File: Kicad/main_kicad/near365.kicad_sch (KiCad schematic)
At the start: 34 parts, among them J1 BMS power input, J2 USB_C_Receptacle_USB2.0_16P, SW1 Switch, SW2 Switch, SW3 SW_en, SW4 SW_boot, SW5 RotaryEncoder_Switch_MP, U1 ESP32-S3-WROOM-1, U2 TC00500, U3 CR2013-MI2120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

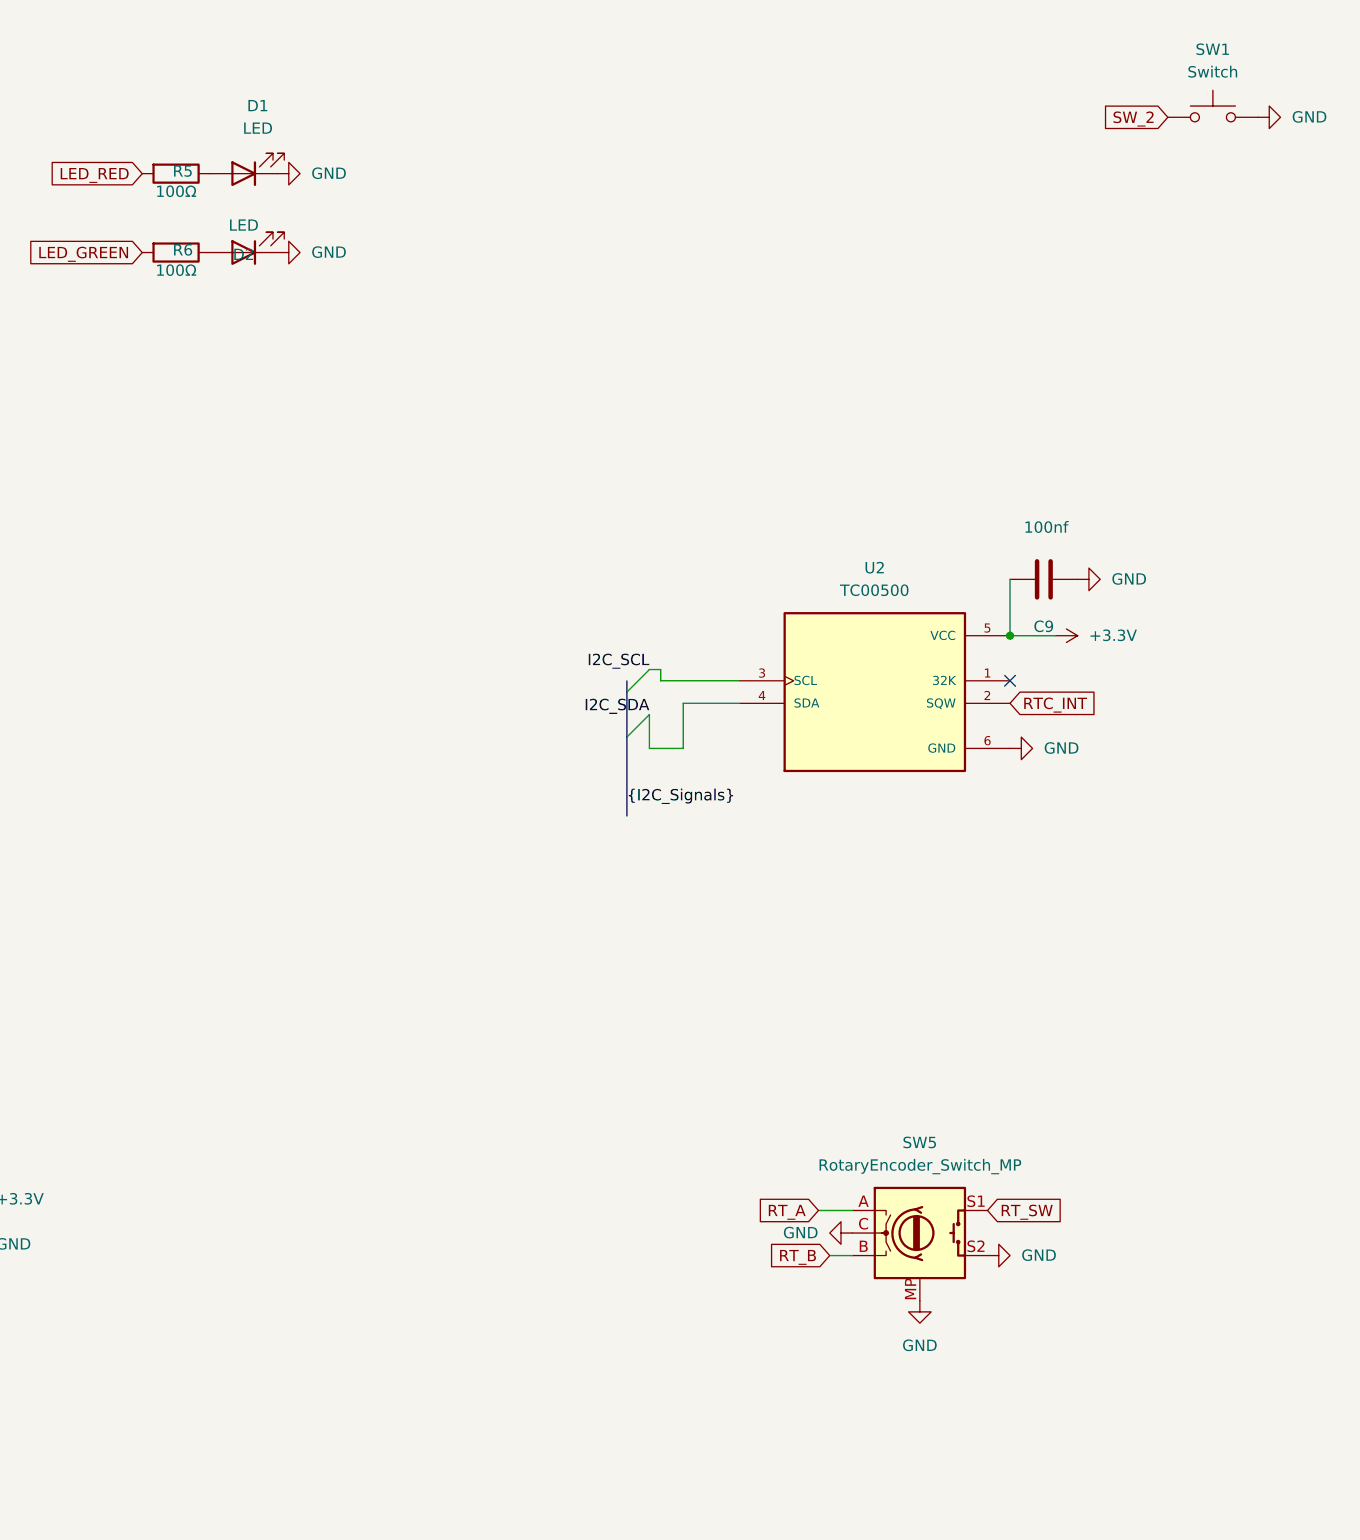
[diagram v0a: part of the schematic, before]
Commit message: Updated power, made changes to 3d front plate, added pull down r to encoder
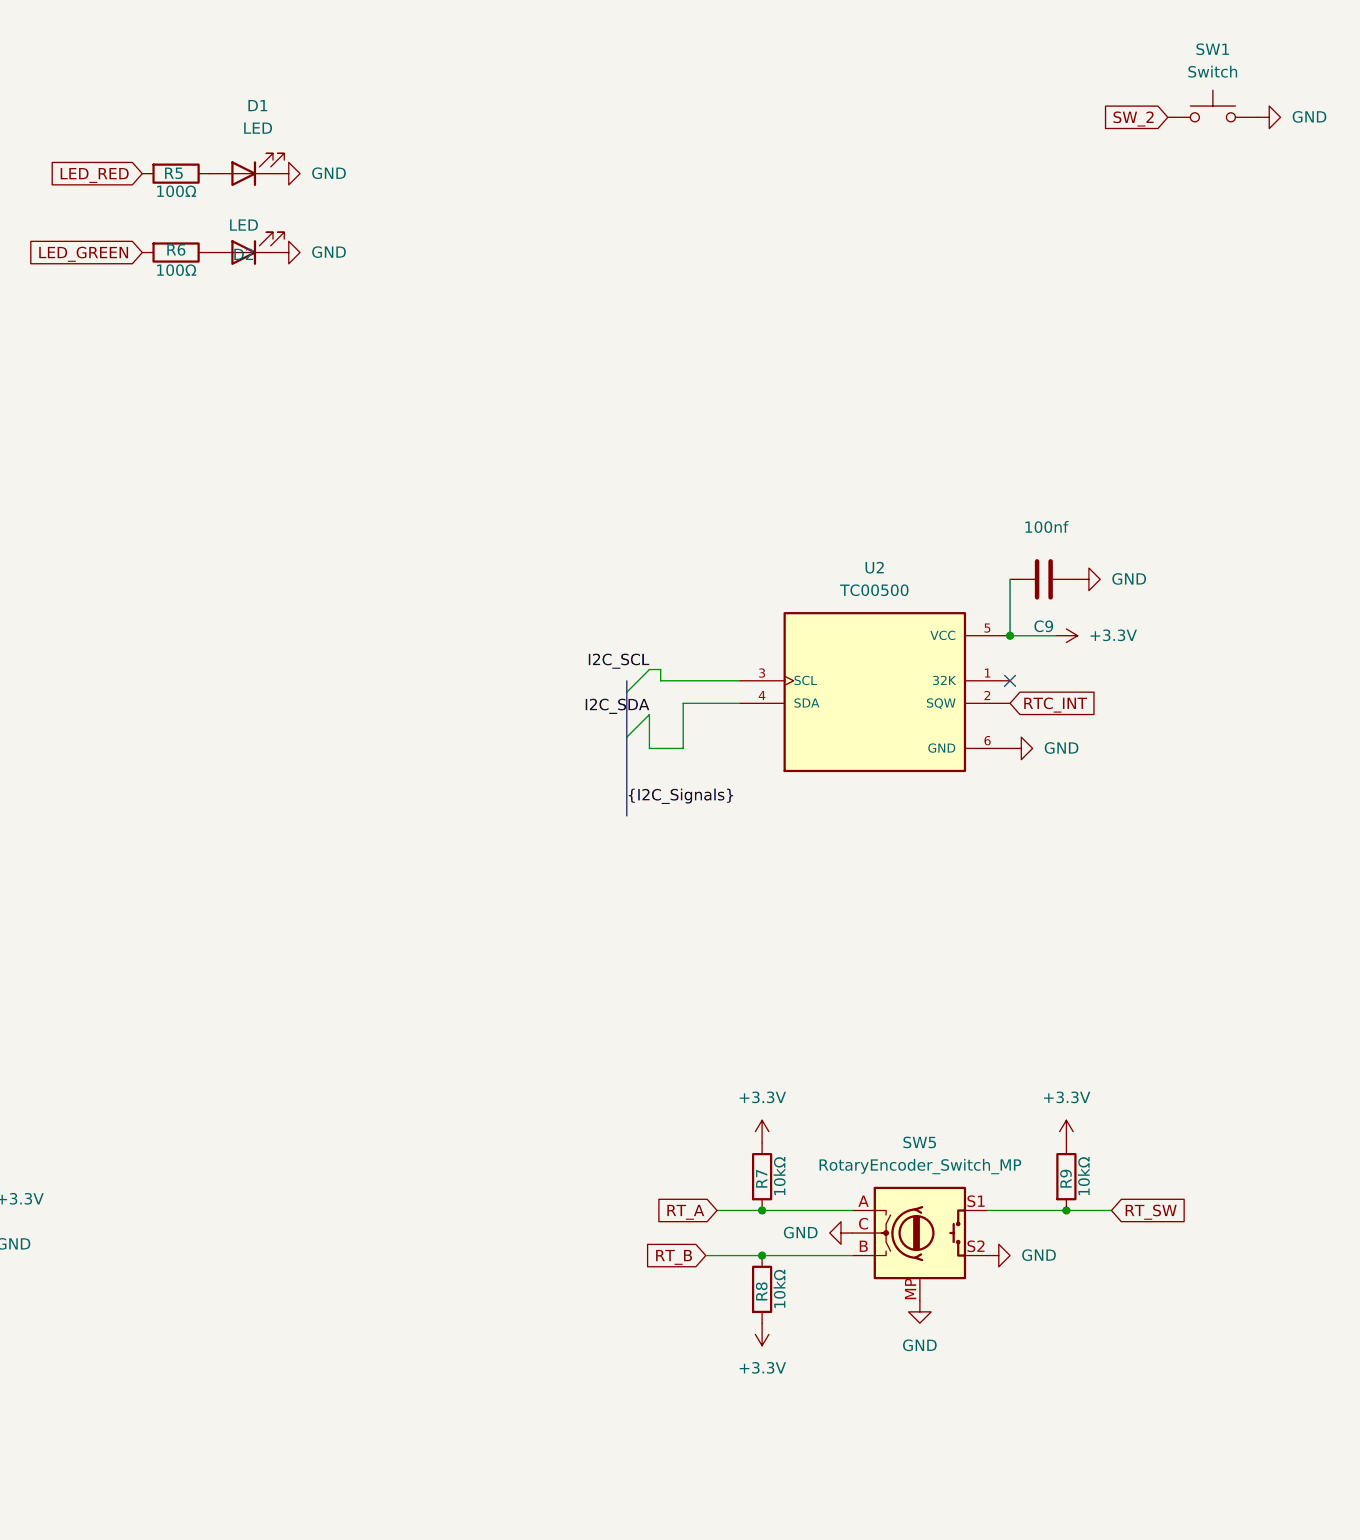
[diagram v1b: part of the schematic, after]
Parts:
- added R7, R8, R9: 10kΩ, Resistor_THT:R_Axial_DIN0207_L6.3mm_D2.5mm_P7.62mm_Horizontal, symbol ScottoKeebs:Placeholder_Resistor
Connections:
- net +3.3V: now also R7.1, R8.2, R9.1
- net RT_A: now also R7.2
- net RT_B: now also R8.1
- net RT_SW: now also R9.2
